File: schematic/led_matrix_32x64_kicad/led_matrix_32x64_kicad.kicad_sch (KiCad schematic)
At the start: 11 parts, among them J1 LED Interface, J2 RTC, J3 INTERFACE, J4 LEDPWR, SW3 RESET, U1 Pico, U2 NCP380

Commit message: Passing ERC and DRC checks
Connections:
- net GND: now also U2.2 (GND)
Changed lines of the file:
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@@
   (junction (at 156.845 62.865) (diameter 0) (color 0 0 0 0)
+  )
+  (junction (at 163.195 65.405) (diameter 0) (color 0 0 0 0)
   )
   (junction (at 160.655 62.865) (diameter 0) (color 0 0 0 0)
@@
   )
   (wire (pts (xy 149.86 140.97) (xy 154.94 140.97))
+    (stroke (width 0) (type default) (color 0 0 0 0))
+  )
+  (wire (pts (xy 163.195 65.405) (xy 170.815 65.405))
     (stroke (width 0) (type default) (color 0 0 0 0))
   )
@@
     (stroke (width 0) (type default) (color 0 0 0 0))
   )
-  (wire (pts (xy 163.195 58.42) (xy 163.195 70.485))
+  (wire (pts (xy 163.195 58.42) (xy 163.195 65.405))
     (stroke (width 0) (type default) (color 0 0 0 0))
   )
@@
     (stroke (width 0) (type default) (color 0 0 0 0))
   )
+  (wire (pts (xy 163.195 65.405) (xy 163.195 70.485))
+    (stroke (width 0) (type default) (color 0 0 0 0))
+  )

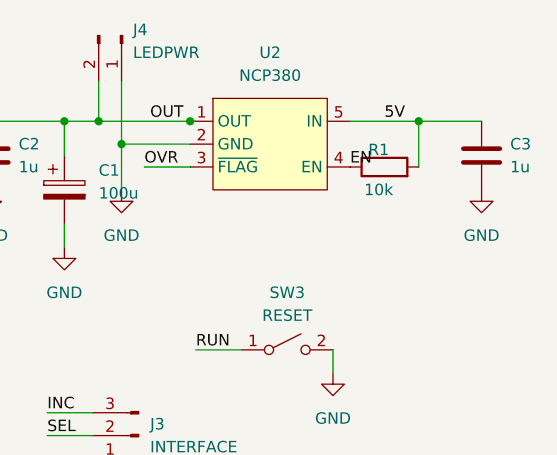
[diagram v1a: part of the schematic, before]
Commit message: update kicad schematin to tie MCP380 enable to ground
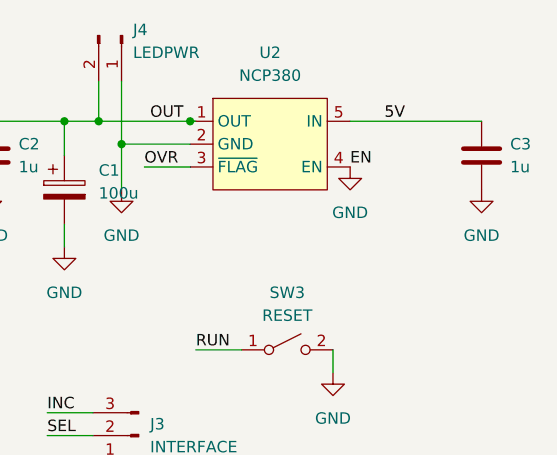
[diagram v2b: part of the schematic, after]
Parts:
- removed R1: 10k, Resistor_SMD:R_0805_2012Metric_Pad1.20x1.40mm_HandSolder, symbol Device:R
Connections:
- net EN is gone; now on net GND: U2.4 (EN)
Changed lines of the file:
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@@
     (company "Matt Wachowski")
-  )
-  (junction (at 196.215 62.865) (diameter 0) (color 0 0 0 0)
   )
   (junction (at 170.815 62.865) (diameter 0) (color 0 0 0 0)
@@
     (stroke (width 0) (type default) (color 0 0 0 0))
   )
-  (wire (pts (xy 196.215 62.865) (xy 203.2 62.865))
-    (stroke (width 0) (type default) (color 0 0 0 0))
-  )
   (wire (pts (xy 167.64 135.89) (xy 173.99 135.89))
     (stroke (width 0) (type default) (color 0 0 0 0))
@@
     (stroke (width 0) (type default) (color 0 0 0 0))
   )
-  (wire (pts (xy 188.595 62.865) (xy 196.215 62.865))
+  (wire (pts (xy 188.595 62.865) (xy 203.2 62.865))
     (stroke (width 0) (type default) (color 0 0 0 0))
   )
@@
   )
   (wire (pts (xy 128.27 77.47) (xy 136.525 77.47))
-    (stroke (width 0) (type default) (color 0 0 0 0))
-  )
-  (wire (pts (xy 196.215 62.865) (xy 196.215 67.945))
     (stroke (width 0) (type default) (color 0 0 0 0))
   )
@@
     (pin "2")
   )
-  (symbol (lib_id "Device:R") (at 192.405 67.945 90) (unit 1)
-    (in_bom yes) (on_board yes)
-    (property "Reference" "R1" (id 0) (at 191.77 66.04 90))
-    (property "Value" "10k" (id 1) (at 191.77 70.485 90))
-    (property "Footprint" "Resistor_SMD:R_0805_2012Metric_Pad1.20x1.40mm_HandSolder" (id 2) (at 192.405 69.723 90)
-      (effects (font (size 1.27 1.27)) hide)
-    )
-    (property "Datasheet" "~" (id 3) (at 192.405 67.945 0)
-      (effects (font (size 1.27 1.27)) hide)
-    )
-    (pin "1")
-    (pin "2")
-  )
   (symbol (lib_id "power:GND") (at 160.02 103.505 0) (unit 1)
     (in_bom yes) (on_board yes) (fields_autoplaced)
@@
     )
     (property "Datasheet" "" (id 3) (at 177.165 109.855 0)
+      (effects (font (size 1.27 1.27)) hide)
+    )
+    (pin "1")
+  )
+  (symbol (lib_id "power:GND") (at 188.595 67.945 0) (unit 1)
+    (in_bom yes) (on_board yes) (fields_autoplaced)
+    (property "Reference" "#PWR?" (id 0) (at 188.595 74.295 0)
+      (effects (font (size 1.27 1.27)) hide)
+    )
+    (property "Value" "GND" (id 1) (at 188.595 73.025 0))
+    (property "Footprint" "" (id 2) (at 188.595 67.945 0)
+      (effects (font (size 1.27 1.27)) hide)
+    )
+    (property "Datasheet" "" (id 3) (at 188.595 67.945 0)
       (effects (font (size 1.27 1.27)) hide)
     )
@@
       (reference "#PWR0102") (unit 1) (value "GND") (footprint "")
     )
+    (path "/385651d3-9dcf-456f-8879-ceb33e49ef52"
+      (reference "#PWR?") (unit 1) (value "GND") (footprint "")
+    )
     (path "/87e5dc14-ec2c-4db9-b820-3bcc7c160b8a"
       (reference "C1") (unit 1) (value "100u") (footprint "Capacitor_THT:CP_Radial_D6.3mm_P2.50mm")
@@
       (reference "J4") (unit 1) (value "LEDPWR") (footprint "Connector_PinHeader_2.54mm:PinHeader_1x02_P2.54mm_Horizontal")
     )
-    (path "/185642f4-66c6-4e82-9426-bae657300b0c"
-      (reference "R1") (unit 1) (value "10k") (footprint "Resistor_SMD:R_0805_2012Metric_Pad1.20x1.40mm_HandSolder")
-    )
     (path "/f91c723a-0bca-4356-9537-04c9b611b4f3"
